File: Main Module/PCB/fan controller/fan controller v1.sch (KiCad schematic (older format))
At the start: 9 parts

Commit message: * working on fan controller PCB
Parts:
- removed P?: FAN Connector, symbol CONN_01X02
- removed U?: OPTO-TRANSISTOR-4, symbol OPTO-TRANSISTOR-4
- added P3: FAN, Pin_Headers:Pin_Header_Straight_1x03, symbol CONN_01X03
- added U1: Octocoupler, Housings_DIP:DIP-4_W7.62mm_LongPads, symbol TLP785
- 1.4K1: renamed from 1.4K; footprint (none) -> Resistors_ThroughHole:Resistor_Horizontal_RM7mm
- 10K1: renamed from 10K; footprint (none) -> Resistors_ThroughHole:Resistor_Horizontal_RM7mm
- 1K1: renamed from 1K; value R -> 1K; footprint (none) -> Resistors_ThroughHole:Resistor_Horizontal_RM7mm
- 1K2: renamed from 1K; footprint (none) -> Resistors_ThroughHole:Resistor_Horizontal_RM7mm
- P1: renamed from P?; value AUX1-3 -> AUX; footprint (none) -> MOBB-KiCad-Lib:Screw_Terminal_5mm
- P2: renamed from P?; footprint (none) -> MOBB-KiCad-Lib:Screw_Terminal_5mm
- Q1: renamed from Q?; value Q_NPN_CBE -> NPN; footprint (none) -> TO_SOT_Packages_THT:TO-92_Inline_Narrow_Oval
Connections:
- net +12V: now also P3.2 (P2)
- net GND: no longer P1.1 (P1), Q1.1 (C)
- net at 1K1.1: now also U1.1
- net at 10K1.2, Q1.2 (B): now also U1.3
- net at 1K2.2: now also 1.4K1.2, U1.4
- new net: P3.1 (P1), P3.3 (P3), Q1.1 (C)
- new net GNDA: P1.1 (P1), U1.2
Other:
- moved on the sheet: P1, P2
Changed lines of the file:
@@
 LIBS:contrib
 LIBS:valves
+LIBS:fan controller v1-cache
 EELAYER 25 0
 EELAYER END
@@
 $EndDescr
 $Comp
-L CONN_01X02 P?
+L CONN_01X02 P1
 U 1 1 57F24616
-P 1850 3400
-F 0 "P?" H 1850 3550 50  0000 C CNN
-F 1 "AUX1-3" V 1950 3400 50  0000 C CNN
-F 2 "" H 1850 3400 50  0000 C CNN
-F 3 "" H 1850 3400 50  0000 C CNN
-	1    1850 3400
+P 1550 3450
+F 0 "P1" H 1550 3600 50  0000 C CNN
+F 1 "AUX" V 1650 3450 50  0000 C CNN
+F 2 "MOBB-KiCad-Lib:Screw_Terminal_5mm" H 1550 3450 50  0001 C CNN
+F 3 "" H 1550 3450 50  0000 C CNN
+	1    1550 3450
 	-1   0    0    1
 $EndComp
 $Comp
-L OPTO-TRANSISTOR-4 U?
-U 1 1 57F2479B
-P 3100 3450
-F 0 "U?" H 2900 3650 50  0000 L CNN
-F 1 "OPTO-TRANSISTOR-4" H 2900 3250 50  0000 L CNN
-F 2 "" H 2900 3250 50  0000 L CIN
-F 3 "" H 3100 3450 50  0000 L CNN
-	1    3100 3450
-	1    0    0    -1
-$EndComp
-$Comp
-L R 1K
+L R 1K1
 U 1 1 57F247E8
 P 2500 3350
-F 0 "1K" V 2580 3350 50  0000 C CNN
-F 1 "R" V 2500 3350 50  0000 C CNN
-F 2 "" V 2430 3350 50  0000 C CNN
+F 0 "1K1" V 2580 3350 50  0000 C CNN
+F 1 "1K" V 2500 3350 50  0000 C CNN
+F 2 "Resistors_ThroughHole:Resistor_Horizontal_RM7mm" V 2430 3350 50  0001 C CNN
 F 3 "" H 2500 3350 50  0000 C CNN
 	1    2500 3350
@@
 $EndComp
 Wire Wire Line
-	2050 3350 2350 3350
-Wire Wire Line
 	2650 3350 2800 3350
-Wire Wire Line
-	2050 3550 2800 3550
-$Comp
-L R 1.4K
+$Comp
+L R 1.4K1
 U 1 1 57F248FE
 P 3550 2950
-F 0 "1.4K" V 3630 2950 50  0000 C CNN
+F 0 "1.4K1" V 3630 2950 50  0000 C CNN
 F 1 "R" V 3550 2950 50  0000 C CNN
-F 2 "" V 3480 2950 50  0000 C CNN
+F 2 "Resistors_ThroughHole:Resistor_Horizontal_RM7mm" V 3480 2950 50  0001 C CNN
 F 3 "" H 3550 2950 50  0000 C CNN
 	1    3550 2950
@@
 $EndComp
 $Comp
-L R 1K
+L R 1K2
 U 1 1 57F249B1
 P 3800 3100
-F 0 "1K" V 3880 3100 50  0000 C CNN
+F 0 "1K2" V 3880 3100 50  0000 C CNN
 F 1 "R" V 3800 3100 50  0000 C CNN
-F 2 "" V 3730 3100 50  0000 C CNN
+F 2 "Resistors_ThroughHole:Resistor_Horizontal_RM7mm" V 3730 3100 50  0001 C CNN
 F 3 "" H 3800 3100 50  0000 C CNN
 	1    3800 3100
@@
 $EndComp
 Wire Wire Line
-	3550 2500 3550 2800
-Wire Wire Line
 	3400 3100 3650 3100
 Wire Wire Line
 	3400 3100 3400 3350
 $Comp
-L Q_NPN_CBE Q?
+L Q_NPN_CBE Q1
 U 1 1 57F24B04
 P 4350 3600
-F 0 "Q?" H 4650 3650 50  0000 R CNN
-F 1 "Q_NPN_CBE" H 4950 3550 50  0000 R CNN
-F 2 "" H 4550 3700 50  0000 C CNN
+F 0 "Q1" H 4650 3650 50  0000 R CNN
+F 1 "NPN" H 4700 3500 50  0000 R CNN
+F 2 "TO_SOT_Packages_THT:TO-92_Inline_Narrow_Oval" H 4550 3700 50  0001 C CNN
 F 3 "" H 4350 3600 50  0000 C CNN
 	1    4350 3600
 	1    0    0    -1
 $EndComp
-Wire Wire Line
-	3550 2700 4400 2700
-Connection ~ 3550 2700
-$Comp
-L CONN_01X02 P?
-U 1 1 57F24BA5
-P 4600 2750
-F 0 "P?" H 4600 2900 50  0000 C CNN
-F 1 "FAN Connector" V 4700 2750 50  0000 C CNN
-F 2 "" H 4600 2750 50  0000 C CNN
-F 3 "" H 4600 2750 50  0000 C CNN
-	1    4600 2750
-	1    0    0    -1
-$EndComp
-$Comp
-L CONN_01X02 P?
+$Comp
+L CONN_01X02 P2
 U 1 1 57F24C78
-P 3600 2300
-F 0 "P?" H 3600 2450 50  0000 C CNN
-F 1 "+12V Suppply" V 3700 2300 50  0000 C CNN
-F 2 "" H 3600 2300 50  0000 C CNN
-F 3 "" H 3600 2300 50  0000 C CNN
-	1    3600 2300
+P 3750 1850
+F 0 "P2" H 3750 2000 50  0000 C CNN
+F 1 "+12V Suppply" V 3850 1850 50  0000 C CNN
+F 2 "MOBB-KiCad-Lib:Screw_Terminal_5mm" H 3750 1850 50  0001 C CNN
+F 3 "" H 3750 1850 50  0000 C CNN
+	1    3750 1850
 	0    -1   -1   0
 $EndComp
-Text Label 3550 2700 1    60   ~ 0
-+12V
-Wire Wire Line
-	3650 2500 3950 2500
-Wire Wire Line
-	3950 2500 3950 3900
-Text Label 3700 2500 0    60   ~ 0
-GND
-Text Label 4450 3000 1    60   ~ 0
-GND
-Text Label 4200 2700 0    60   ~ 0
-+12V
-Text Label 2100 3550 0    60   ~ 0
-GND
-Wire Wire Line
-	2050 3450 2050 3550
-Text Label 2100 3350 0    60   ~ 0
-+5V
-$Comp
-L R 10K
+Wire Wire Line
+	3950 2050 3950 3900
+$Comp
+L R 10K1
 U 1 1 57F24F38
 P 4100 3750
-F 0 "10K" V 4180 3750 50  0000 C CNN
+F 0 "10K1" V 4180 3750 50  0000 C CNN
 F 1 "R" V 4100 3750 50  0000 C CNN
-F 2 "" V 4030 3750 50  0000 C CNN
+F 2 "Resistors_ThroughHole:Resistor_Horizontal_RM7mm" V 4030 3750 50  0001 C CNN
 F 3 "" H 4100 3750 50  0000 C CNN
 	1    4100 3750
@@
 	4450 3900 4450 3800
 Connection ~ 4100 3900
-Wire Wire Line
-	4450 3400 4450 2800
-Wire Wire Line
-	4450 2800 4400 2800
+$Comp
+L +5V #PWR01
+U 1 1 581A5A6C
+P 1750 3250
+F 0 "#PWR01" H 1750 3100 50  0001 C CNN
+F 1 "+5V" H 1750 3390 50  0000 C CNN
+F 2 "" H 1750 3250 50  0000 C CNN
+F 3 "" H 1750 3250 50  0000 C CNN
+	1    1750 3250
+	1    0    0    -1
+$EndComp
+$Comp
+L GNDA #PWR02
+U 1 1 581A5A92
+P 1750 3600
+F 0 "#PWR02" H 1750 3350 50  0001 C CNN
+F 1 "GNDA" H 1750 3450 50  0000 C CNN
+F 2 "" H 1750 3600 50  0000 C CNN
+F 3 "" H 1750 3600 50  0000 C CNN
+	1    1750 3600
+	1    0    0    -1
+$EndComp
+Wire Wire Line
+	1750 3500 1750 3600
+Wire Wire Line
+	1750 3250 1750 3400
+$Comp
+L +12V #PWR03
+U 1 1 581A5D1A
+P 3450 2050
+F 0 "#PWR03" H 3450 1900 50  0001 C CNN
+F 1 "+12V" H 3450 2190 50  0000 C CNN
+F 2 "" H 3450 2050 50  0000 C CNN
+F 3 "" H 3450 2050 50  0000 C CNN
+	1    3450 2050
+	0    -1   -1   0
+$EndComp
+$Comp
+L GND #PWR04
+U 1 1 581A5D64
+P 4050 2050
+F 0 "#PWR04" H 4050 1800 50  0001 C CNN
+F 1 "GND" H 4050 1900 50  0000 C CNN
+F 2 "" H 4050 2050 50  0000 C CNN
+F 3 "" H 4050 2050 50  0000 C CNN
+	1    4050 2050
+	0    -1   -1   0
+$EndComp
+Wire Wire Line
+	3450 2050 3700 2050
+Wire Wire Line
+	3800 2050 4050 2050
+Connection ~ 3550 2050
+Connection ~ 3950 2050
+Wire Wire Line
+	2800 3550 1750 3550
+Connection ~ 1750 3550
+Wire Wire Line
+	2350 3350 1750 3350
+Connection ~ 1750 3350
+Connection ~ 3550 3100
+Connection ~ 3450 2050
+Connection ~ 4050 2050
+Connection ~ 1750 3250
+Connection ~ 1750 3600
+$Comp
+L TLP785 U1
+U 1 1 581A6379
+P 3100 3450
+F 0 "U1" H 2900 3650 50  0000 L CNN
+F 1 "Octocoupler" H 2900 3200 50  0000 L CNN
+F 2 "Housings_DIP:DIP-4_W7.62mm_LongPads" H 2900 3250 50  0000 L CIN
+F 3 "" H 3100 3450 50  0000 L CNN
+	1    3100 3450
+	1    0    0    -1
+$EndComp
+$Comp
+L CONN_01X03 P3
+U 1 1 581A85A6
+P 5000 2700
+F 0 "P3" H 5000 2900 50  0000 C CNN
+F 1 "FAN" V 5100 2700 50  0000 C CNN
+F 2 "Pin_Headers:Pin_Header_Straight_1x03" H 5000 2700 50  0001 C CNN
+F 3 "" H 5000 2700 50  0000 C CNN
+	1    5000 2700
+	1    0    0    -1
+$EndComp
+Wire Wire Line
+	3550 2050 3550 2800
+Wire Wire Line
+	4800 2700 3550 2700
+Connection ~ 3550 2700
+Wire Wire Line
+	4450 2600 4800 2600
+Wire Wire Line
+	4450 3400 4450 2600
+Wire Wire Line
+	4800 2800 4450 2800
+Connection ~ 4450 2800
 $EndSCHEMATC

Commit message: * added solder pads for another fan header to the PCB. there is room ... might as well
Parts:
- added P4: Fan, Pin_Headers:Pin_Header_Straight_1x03, symbol CONN_01X03
- P3: value FAN -> Fan
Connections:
- net +12V: now also P4.2 (P2)
- net at P3.1 (P1), P3.3 (P3), Q1.1 (C): now also P4.1 (P1), P4.3 (P3)
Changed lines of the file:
@@
 P 5000 2700
 F 0 "P3" H 5000 2900 50  0000 C CNN
-F 1 "FAN" V 5100 2700 50  0000 C CNN
+F 1 "Fan" V 5100 2700 50  0000 C CNN
 F 2 "Pin_Headers:Pin_Header_Straight_1x03" H 5000 2700 50  0001 C CNN
 F 3 "" H 5000 2700 50  0000 C CNN
@@
 	3550 2050 3550 2800
 Wire Wire Line
-	4800 2700 3550 2700
+	3550 2700 5350 2700
 Connection ~ 3550 2700
 Wire Wire Line
-	4450 2600 4800 2600
+	4450 2600 5350 2600
 Wire Wire Line
 	4450 3400 4450 2600
 Wire Wire Line
-	4800 2800 4450 2800
+	4450 2800 5350 2800
 Connection ~ 4450 2800
+$Comp
+L CONN_01X03 P4
+U 1 1 581B96A9
+P 5550 2700
+F 0 "P4" H 5550 2900 50  0000 C CNN
+F 1 "Fan" V 5650 2700 50  0000 C CNN
+F 2 "Pin_Headers:Pin_Header_Straight_1x03" H 5550 2700 50  0001 C CNN
+F 3 "" H 5550 2700 50  0000 C CNN
+	1    5550 2700
+	1    0    0    -1
+$EndComp
+Connection ~ 4800 2600
+Connection ~ 4800 2700
+Connection ~ 4800 2800
 $EndSCHEMATC

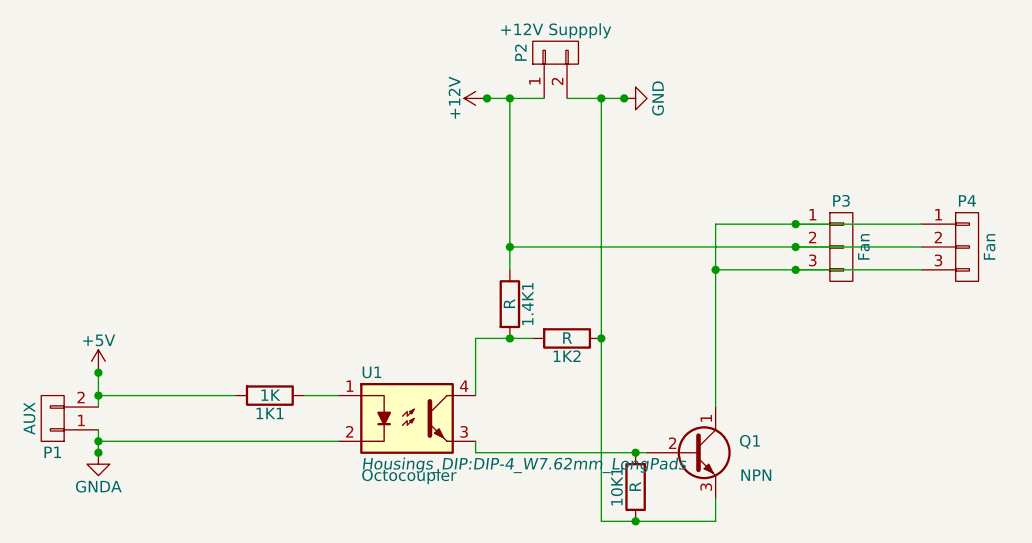
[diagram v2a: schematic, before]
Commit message: * corrected molex connectors on Fan PCB * added optional LED to show "ON" state
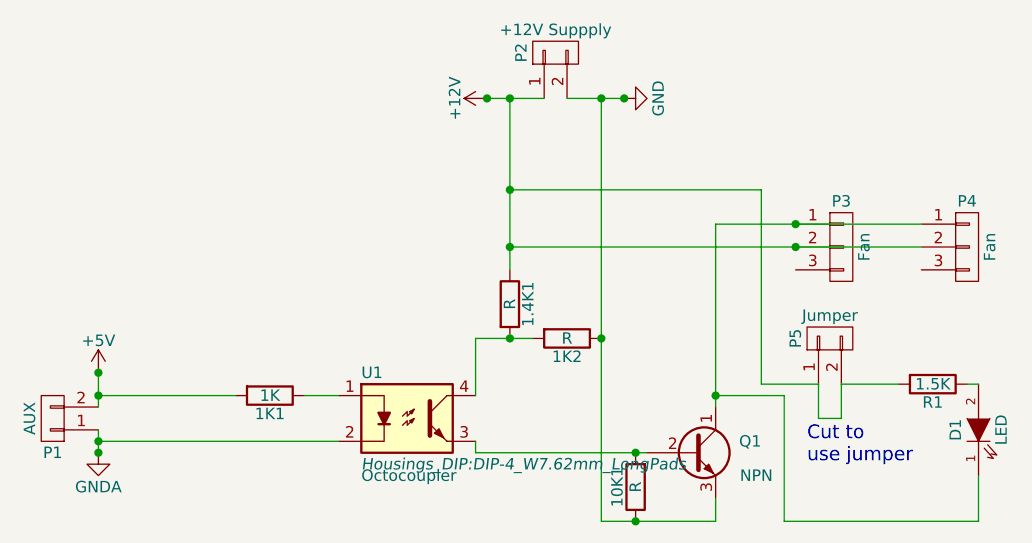
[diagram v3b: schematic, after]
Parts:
- added D1: LED, LEDs:LED-3MM, symbol LED
- added P5: Jumper, Pin_Headers:Pin_Header_Straight_1x02, symbol CONN_01X02
- added R1: 1.5K, Resistors_ThroughHole:Resistor_Horizontal_RM7mm, symbol R
- P3, P4: footprint Pin_Headers:Pin_Header_Straight_1x03 -> MOBB-KiCad-Lib:Molex-KK-1x3P
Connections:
- net +12V: now also P5.1 (P1), P5.2 (P2), R1.2
- net at P3.1 (P1), P4.1 (P1), Q1.1 (C): now also D1.1 (K); no longer P3.3 (P3), P4.3 (P3)
- new net: D1.2 (A), R1.1
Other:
- note added: "Cut to \nuse jumper"
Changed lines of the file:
@@
 	0    1    1    0
 $EndComp
-Wire Wire Line
-	2650 3350 2800 3350
 $Comp
 L R 1.4K1
@@
 	0    1    1    0
 $EndComp
-Wire Wire Line
-	3400 3100 3650 3100
-Wire Wire Line
-	3400 3100 3400 3350
 $Comp
 L Q_NPN_CBE Q1
@@
 	0    -1   -1   0
 $EndComp
-Wire Wire Line
-	3950 2050 3950 3900
 $Comp
 L R 10K1
@@
 	-1   0    0    1
 $EndComp
-Wire Wire Line
-	3400 3600 4150 3600
-Wire Wire Line
-	3400 3600 3400 3550
-Connection ~ 4100 3600
-Wire Wire Line
-	3950 3900 4450 3900
-Connection ~ 3950 3100
-Wire Wire Line
-	4450 3900 4450 3800
-Connection ~ 4100 3900
 $Comp
 L +5V #PWR01
@@
 	1    0    0    -1
 $EndComp
-Wire Wire Line
-	1750 3500 1750 3600
-Wire Wire Line
-	1750 3250 1750 3400
 $Comp
 L +12V #PWR03
@@
 	0    -1   -1   0
 $EndComp
-Wire Wire Line
-	3450 2050 3700 2050
-Wire Wire Line
-	3800 2050 4050 2050
-Connection ~ 3550 2050
-Connection ~ 3950 2050
-Wire Wire Line
-	2800 3550 1750 3550
-Connection ~ 1750 3550
-Wire Wire Line
-	2350 3350 1750 3350
-Connection ~ 1750 3350
-Connection ~ 3550 3100
-Connection ~ 3450 2050
-Connection ~ 4050 2050
-Connection ~ 1750 3250
-Connection ~ 1750 3600
 $Comp
 L TLP785 U1
@@
 F 0 "P3" H 5000 2900 50  0000 C CNN
 F 1 "Fan" V 5100 2700 50  0000 C CNN
-F 2 "Pin_Headers:Pin_Header_Straight_1x03" H 5000 2700 50  0001 C CNN
+F 2 "MOBB-KiCad-Lib:Molex-KK-1x3P" H 5000 2700 50  0001 C CNN
 F 3 "" H 5000 2700 50  0000 C CNN
 	1    5000 2700
 	1    0    0    -1
 $EndComp
-Wire Wire Line
-	3550 2050 3550 2800
-Wire Wire Line
-	3550 2700 5350 2700
-Connection ~ 3550 2700
-Wire Wire Line
-	4450 2600 5350 2600
-Wire Wire Line
-	4450 3400 4450 2600
-Wire Wire Line
-	4450 2800 5350 2800
-Connection ~ 4450 2800
 $Comp
 L CONN_01X03 P4
@@
 F 0 "P4" H 5550 2900 50  0000 C CNN
 F 1 "Fan" V 5650 2700 50  0000 C CNN
-F 2 "Pin_Headers:Pin_Header_Straight_1x03" H 5550 2700 50  0001 C CNN
+F 2 "MOBB-KiCad-Lib:Molex-KK-1x3P" H 5550 2700 50  0001 C CNN
 F 3 "" H 5550 2700 50  0000 C CNN
 	1    5550 2700
 	1    0    0    -1
 $EndComp
+$Comp
+L R R1
+U 1 1 581F2CCC
+P 5400 3300
+F 0 "R1" V 5480 3300 50  0000 C CNN
+F 1 "1.5K" V 5400 3300 50  0000 C CNN
+F 2 "Resistors_ThroughHole:Resistor_Horizontal_RM7mm" V 5330 3300 50  0001 C CNN
+F 3 "" H 5400 3300 50  0000 C CNN
+	1    5400 3300
+	0    1    1    0
+$EndComp
+$Comp
+L LED D1
+U 1 1 581F2E6E
+P 5600 3500
+F 0 "D1" H 5600 3600 50  0000 C CNN
+F 1 "LED" H 5600 3400 50  0000 C CNN
+F 2 "LEDs:LED-3MM" H 5600 3500 50  0001 C CNN
+F 3 "" H 5600 3500 50  0000 C CNN
+	1    5600 3500
+	0    -1   -1   0
+$EndComp
+Wire Wire Line
+	2650 3350 2800 3350
+Wire Wire Line
+	3400 3100 3650 3100
+Wire Wire Line
+	3400 3100 3400 3350
+Wire Wire Line
+	3950 2050 3950 3900
+Wire Wire Line
+	3400 3600 4150 3600
+Wire Wire Line
+	3400 3600 3400 3550
+Connection ~ 4100 3600
+Connection ~ 3950 3100
+Wire Wire Line
+	4450 3900 4450 3800
+Connection ~ 4100 3900
+Wire Wire Line
+	1750 3500 1750 3600
+Wire Wire Line
+	1750 3250 1750 3400
+Wire Wire Line
+	3450 2050 3700 2050
+Wire Wire Line
+	3800 2050 4050 2050
+Connection ~ 3550 2050
+Connection ~ 3950 2050
+Wire Wire Line
+	2800 3550 1750 3550
+Connection ~ 1750 3550
+Wire Wire Line
+	2350 3350 1750 3350
+Connection ~ 1750 3350
+Connection ~ 3550 3100
+Connection ~ 3450 2050
+Connection ~ 4050 2050
+Connection ~ 1750 3250
+Connection ~ 1750 3600
+Wire Wire Line
+	3550 2050 3550 2800
+Wire Wire Line
+	3550 2700 5350 2700
+Connection ~ 3550 2700
+Wire Wire Line
+	4450 2600 5350 2600
 Connection ~ 4800 2600
 Connection ~ 4800 2700
-Connection ~ 4800 2800
+Wire Wire Line
+	5600 3900 5600 3700
+Wire Wire Line
+	5600 3300 5550 3300
+$Comp
+L CONN_01X02 P5
+U 1 1 581F3210
+P 4950 3100
+F 0 "P5" H 4950 3250 50  0000 C CNN
+F 1 "Jumper" V 5050 3100 50  0000 C CNN
+F 2 "Pin_Headers:Pin_Header_Straight_1x02" H 4950 3100 50  0001 C CNN
+F 3 "" H 4950 3100 50  0000 C CNN
+	1    4950 3100
+	0    -1   -1   0
+$EndComp
+Wire Wire Line
+	5250 3300 5000 3300
+Wire Wire Line
+	4900 3300 4900 3450
+Wire Wire Line
+	4900 3450 5000 3450
+Wire Wire Line
+	5000 3450 5000 3300
+Wire Wire Line
+	3950 3900 4450 3900
+Wire Wire Line
+	4900 3300 4650 3300
+Wire Wire Line
+	4650 3300 4650 2450
+Wire Wire Line
+	4650 2450 3550 2450
+Connection ~ 3550 2450
+Wire Wire Line
+	4450 3400 4450 2600
+Wire Wire Line
+	5600 3900 4750 3900
+Wire Wire Line
+	4750 3900 4750 3350
+Wire Wire Line
+	4750 3350 4450 3350
+Connection ~ 4450 3350
+Text Notes 4850 3650 0    60   ~ 0
+Cut to \nuse jumper
 $EndSCHEMATC

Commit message: * fixed values in schematic
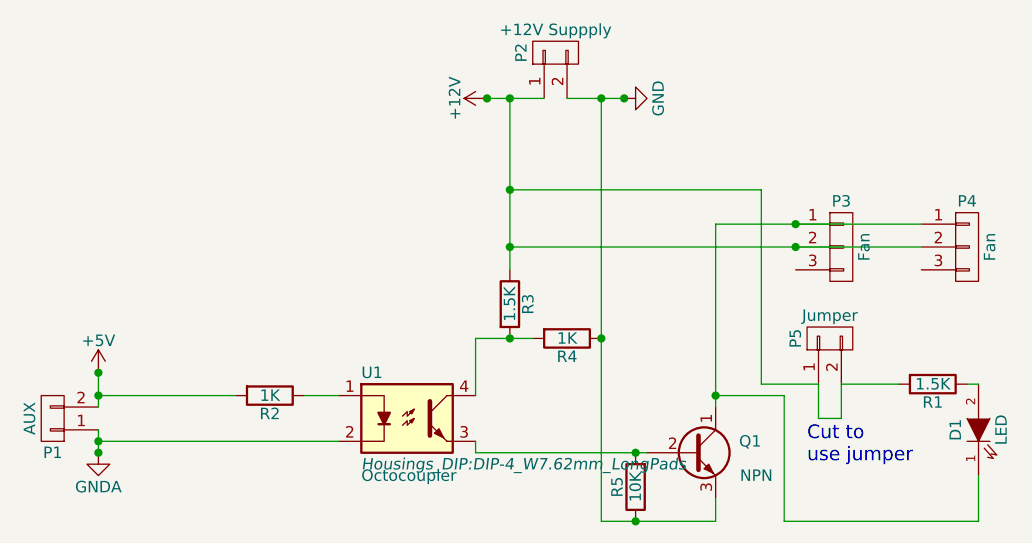
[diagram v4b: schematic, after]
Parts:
- R3: renamed from 1.4K1; value R -> 1.5K
- R4: renamed from 1K2; value R -> 1K
- R5: renamed from 10K1; value R -> 10K
- renumbered 1K1 to R2
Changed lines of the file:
@@
 $EndComp
 $Comp
-L R 1K1
+L R R2
 U 1 1 57F247E8
 P 2500 3350
-F 0 "1K1" V 2580 3350 50  0000 C CNN
+F 0 "R2" V 2580 3350 50  0000 C CNN
 F 1 "1K" V 2500 3350 50  0000 C CNN
 F 2 "Resistors_ThroughHole:Resistor_Horizontal_RM7mm" V 2430 3350 50  0001 C CNN
@@
 $EndComp
 $Comp
-L R 1.4K1
+L R R3
 U 1 1 57F248FE
 P 3550 2950
-F 0 "1.4K1" V 3630 2950 50  0000 C CNN
-F 1 "R" V 3550 2950 50  0000 C CNN
+F 0 "R3" V 3630 2950 50  0000 C CNN
+F 1 "1.5K" V 3550 2950 50  0000 C CNN
 F 2 "Resistors_ThroughHole:Resistor_Horizontal_RM7mm" V 3480 2950 50  0001 C CNN
 F 3 "" H 3550 2950 50  0000 C CNN
@@
 $EndComp
 $Comp
-L R 1K2
+L R R4
 U 1 1 57F249B1
 P 3800 3100
-F 0 "1K2" V 3880 3100 50  0000 C CNN
-F 1 "R" V 3800 3100 50  0000 C CNN
+F 0 "R4" V 3880 3100 50  0000 C CNN
+F 1 "1K" V 3800 3100 50  0000 C CNN
 F 2 "Resistors_ThroughHole:Resistor_Horizontal_RM7mm" V 3730 3100 50  0001 C CNN
 F 3 "" H 3800 3100 50  0000 C CNN
@@
 $EndComp
 $Comp
-L R 10K1
+L R R5
 U 1 1 57F24F38
 P 4100 3750
-F 0 "10K1" V 4180 3750 50  0000 C CNN
-F 1 "R" V 4100 3750 50  0000 C CNN
+F 0 "R5" V 4180 3750 50  0000 C CNN
+F 1 "10K" V 4100 3750 50  0000 C CNN
 F 2 "Resistors_ThroughHole:Resistor_Horizontal_RM7mm" V 4030 3750 50  0001 C CNN
 F 3 "" H 4100 3750 50  0000 C CNN
@@
 $EndComp
 $Comp
-L +5V #PWR01
+L +5V #PWR1
 U 1 1 581A5A6C
 P 1750 3250
-F 0 "#PWR01" H 1750 3100 50  0001 C CNN
+F 0 "#PWR1" H 1750 3100 50  0001 C CNN
 F 1 "+5V" H 1750 3390 50  0000 C CNN
 F 2 "" H 1750 3250 50  0000 C CNN
@@
 $EndComp
 $Comp
-L GNDA #PWR02
+L GNDA #PWR2
 U 1 1 581A5A92
 P 1750 3600
-F 0 "#PWR02" H 1750 3350 50  0001 C CNN
+F 0 "#PWR2" H 1750 3350 50  0001 C CNN
 F 1 "GNDA" H 1750 3450 50  0000 C CNN
 F 2 "" H 1750 3600 50  0000 C CNN
@@
 $EndComp
 $Comp
-L +12V #PWR03
+L +12V #PWR3
 U 1 1 581A5D1A
 P 3450 2050
-F 0 "#PWR03" H 3450 1900 50  0001 C CNN
+F 0 "#PWR3" H 3450 1900 50  0001 C CNN
 F 1 "+12V" H 3450 2190 50  0000 C CNN
 F 2 "" H 3450 2050 50  0000 C CNN
@@
 $EndComp
 $Comp
-L GND #PWR04
+L GND #PWR4
 U 1 1 581A5D64
 P 4050 2050
-F 0 "#PWR04" H 4050 1800 50  0001 C CNN
+F 0 "#PWR4" H 4050 1800 50  0001 C CNN
 F 1 "GND" H 4050 1900 50  0000 C CNN
 F 2 "" H 4050 2050 50  0000 C CNN
